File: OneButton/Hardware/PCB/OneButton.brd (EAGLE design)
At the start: 50.8 x 50.8 mm, 36 parts, among them SW1 DHT-4235A, SW2 DHT-4235A, U1 WS2812, U10 STM32F042GU, U2 WS2812, U3 WS2812, U4 WS2812, U5 WS2812, U6 WS2812, U7 WS2812, U8 WS2812, U9 3.3V

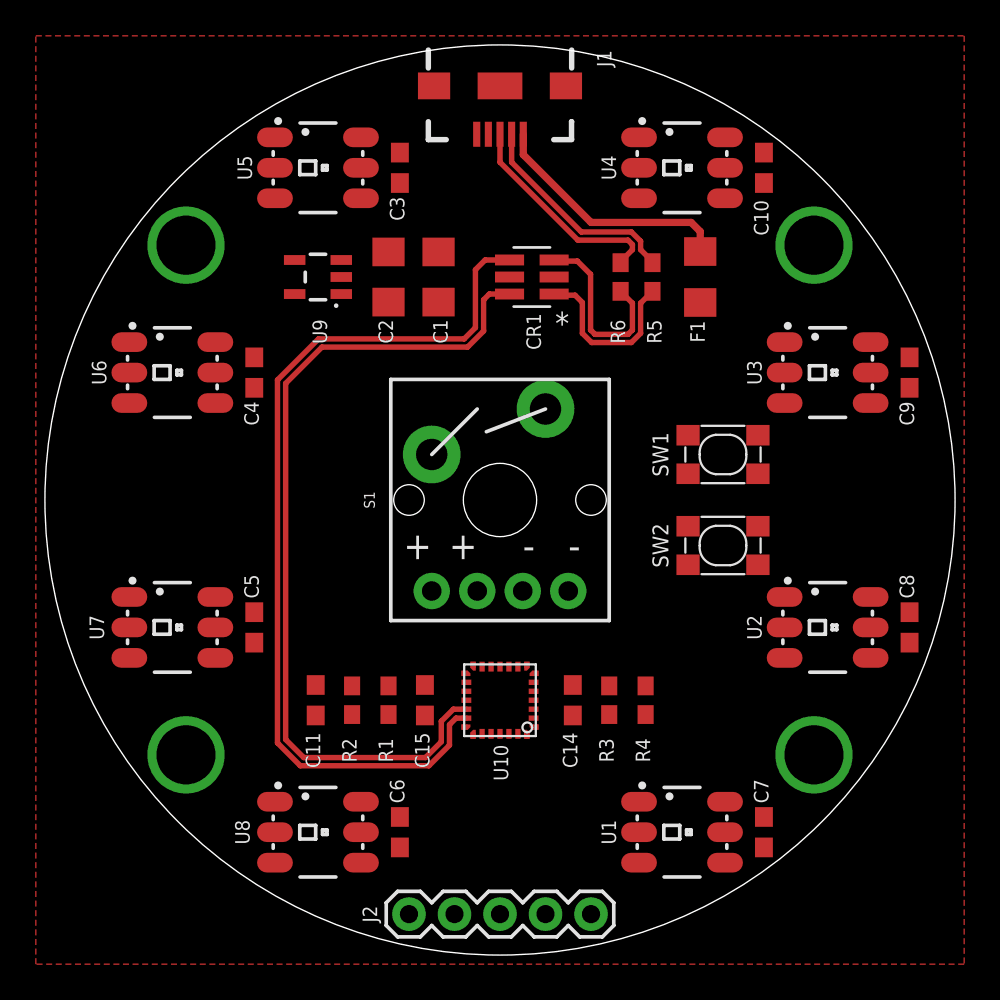
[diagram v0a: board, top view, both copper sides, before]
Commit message: Updated folder structure
Updated folder structure, adding software next
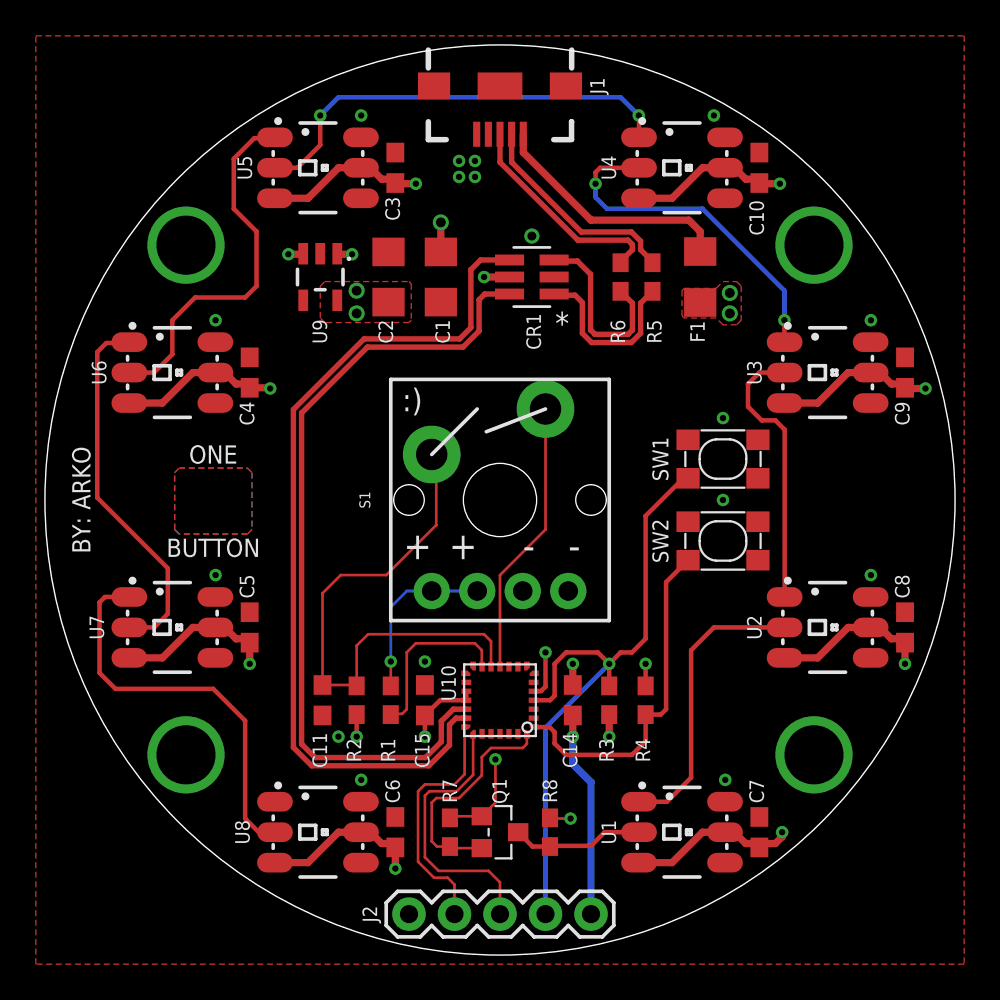
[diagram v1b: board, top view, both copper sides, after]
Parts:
- added Q1: BSS138W-7-F, OneButton:SOT-23
- added R7, R8: 10k, OneButton:RESC0603_N
- moved C11 0.38 mm to (15.5, 14.2)
- moved C3 0.25 mm to (19.6, 43.9)
- moved C6 0.25 mm to (19.6, 6.86)
- moved R2 0.25 mm to (17.4, 14.2)
- moved SW1 0.25 mm to (37.8, 27.7)
- moved SW2 0.25 mm to (37.8, 23.1)
- moved C4 0.25 mm to (11.4, 32.5)
- moved C5 0.25 mm to (11.4, 18.3)
- moved C10 0.25 mm to (39.9, 43.9)
- moved C7 0.25 mm to (39.9, 6.86)
- moved C8 0.25 mm to (48.0, 18.3)
- moved C9 0.25 mm to (48.0, 32.5)
- moved U9 0.13 mm to (15.4, 37.8), turned to 180 degrees
- moved C1 0.13 mm to (22.1, 37.8)
- moved R1 0.13 mm to (19.3, 14.2)
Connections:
- removed net 5V: C14.1, C15.1, C2.1, J2.5, R2.2, R3.2, R4.2, U10.17, U10.18, U10.5, U9.5
- new net 3.3V: C14.1, C15.1, C2.1, J2.5, Q1.1, R2.2, R3.2, R4.2, R7.2, U10.17, U10.18, U10.5, U9.5
- new net N$2: Q1.2, R7.1, U10.28
- net +5V: now also R8.2
- net DAT_IN: now also Q1.3, R8.1; no longer U10.28
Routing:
- net +5V: track 0.00 -> 78.1 mm, vias 0 -> 15
- net RESET: track 0.00 -> 36.0 mm, vias 0 -> 1
- net BUTTON_PIN_1: track 0.00 -> 30.6 mm
- net 3.3V: track 0.00 -> 27.7 mm, vias 0 -> 9
- net N$12: track 0.00 -> 24.6 mm, vias 0 -> 2
- net N$15: track 0.00 -> 22.4 mm
- net N$14: track 0.00 -> 20.7 mm
- net N$13: track 0.00 -> 20.6 mm
- net N$11: track 0.00 -> 19.8 mm, vias 0 -> 2
- net BOOT0: track 0.00 -> 19.1 mm
- net N$9: track 0.00 -> 16.3 mm
- net N$10: track 0.00 -> 15.5 mm
- net BUTTON_PIN_2: track 0.00 -> 15.4 mm
- net SWCLK: track 0.00 -> 15.3 mm
- net SWDIO: track 0.00 -> 13.8 mm
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- added copper zone on layer 1, net +5V
- added copper zone on layer 15, net +5V
- added copper zone on layer 1, net 3.3V
- added copper zone on layer 15, net 3.3V
- added copper zone on layer 1, net N$1
- added copper zone on layer 2, net N$3
- added copper zone on layer 15, net N$4
- added copper zone on layer 16, net N$5
- removed copper zone on layer 15, net 5V
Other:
- board text added: "1"
- board text added: ":)"
- board text added: "BUTTON"
- board text added: "BY: ARKO"
- board text added: "ONE"
